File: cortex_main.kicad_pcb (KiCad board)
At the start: 2 copper layers, 177.8 x 86.4 mm, 7 parts, among them P1 CONN_01X05, P2 CONN_02X04, P3 CONN_01X02, U1 socket_leon_x3_dil64, U2 socket_pololu_24v12, U3 socket_pololu_24v12, U4 socket_lm2596_mod

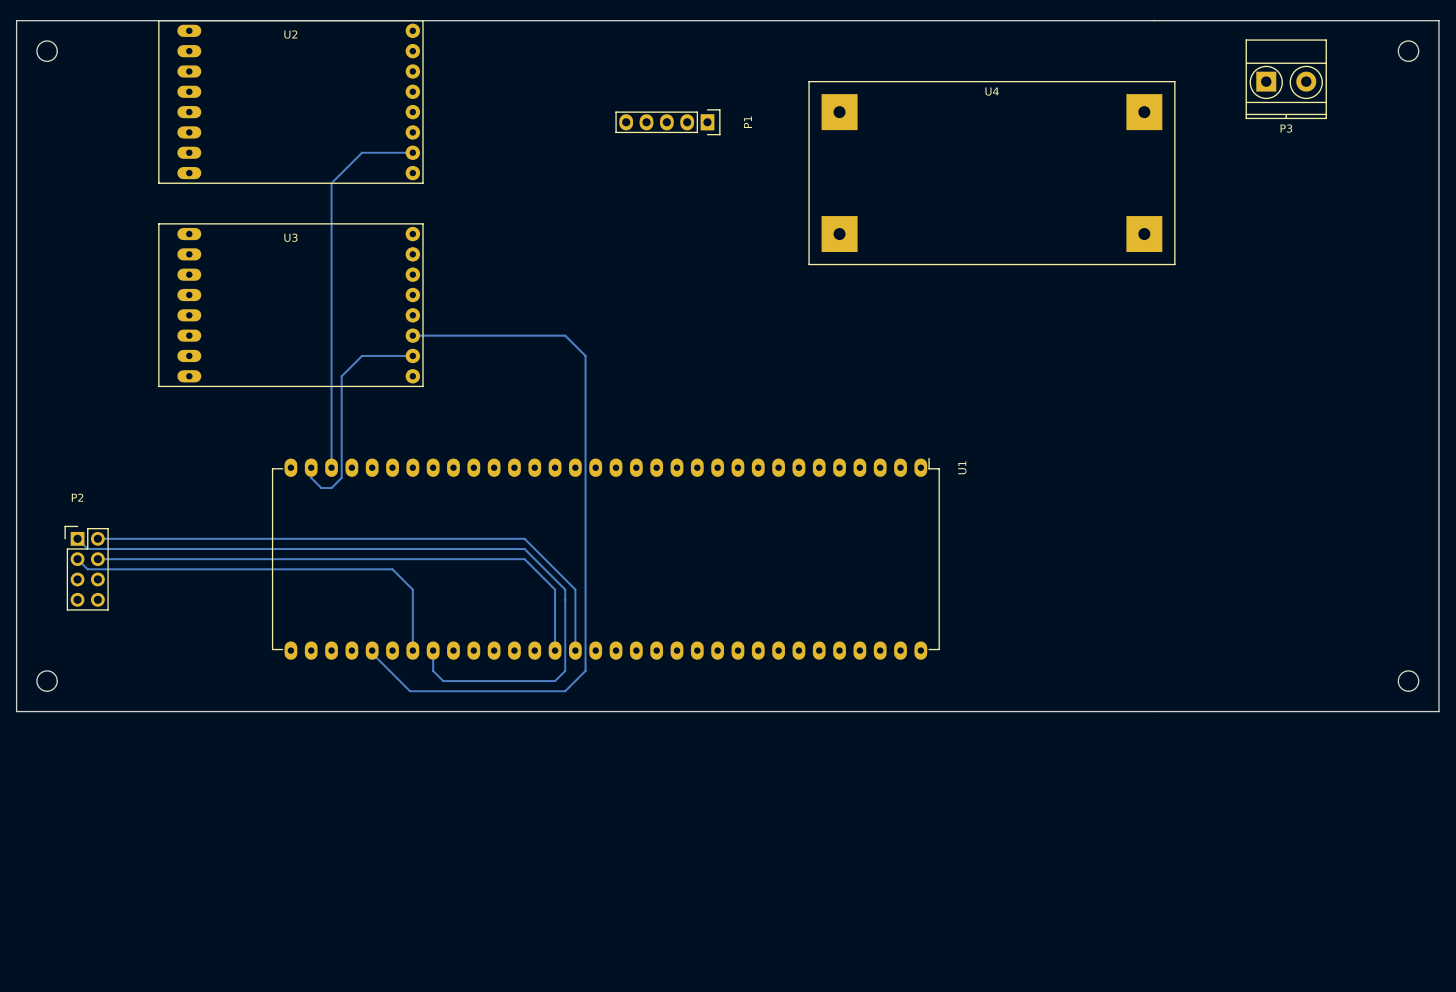
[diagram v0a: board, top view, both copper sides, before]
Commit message: cortex: update to 120x120mm PCB size
To match final mechanical constraints

Signed-off-by: Yannick Gicquel <ygicquel@gmail.com>
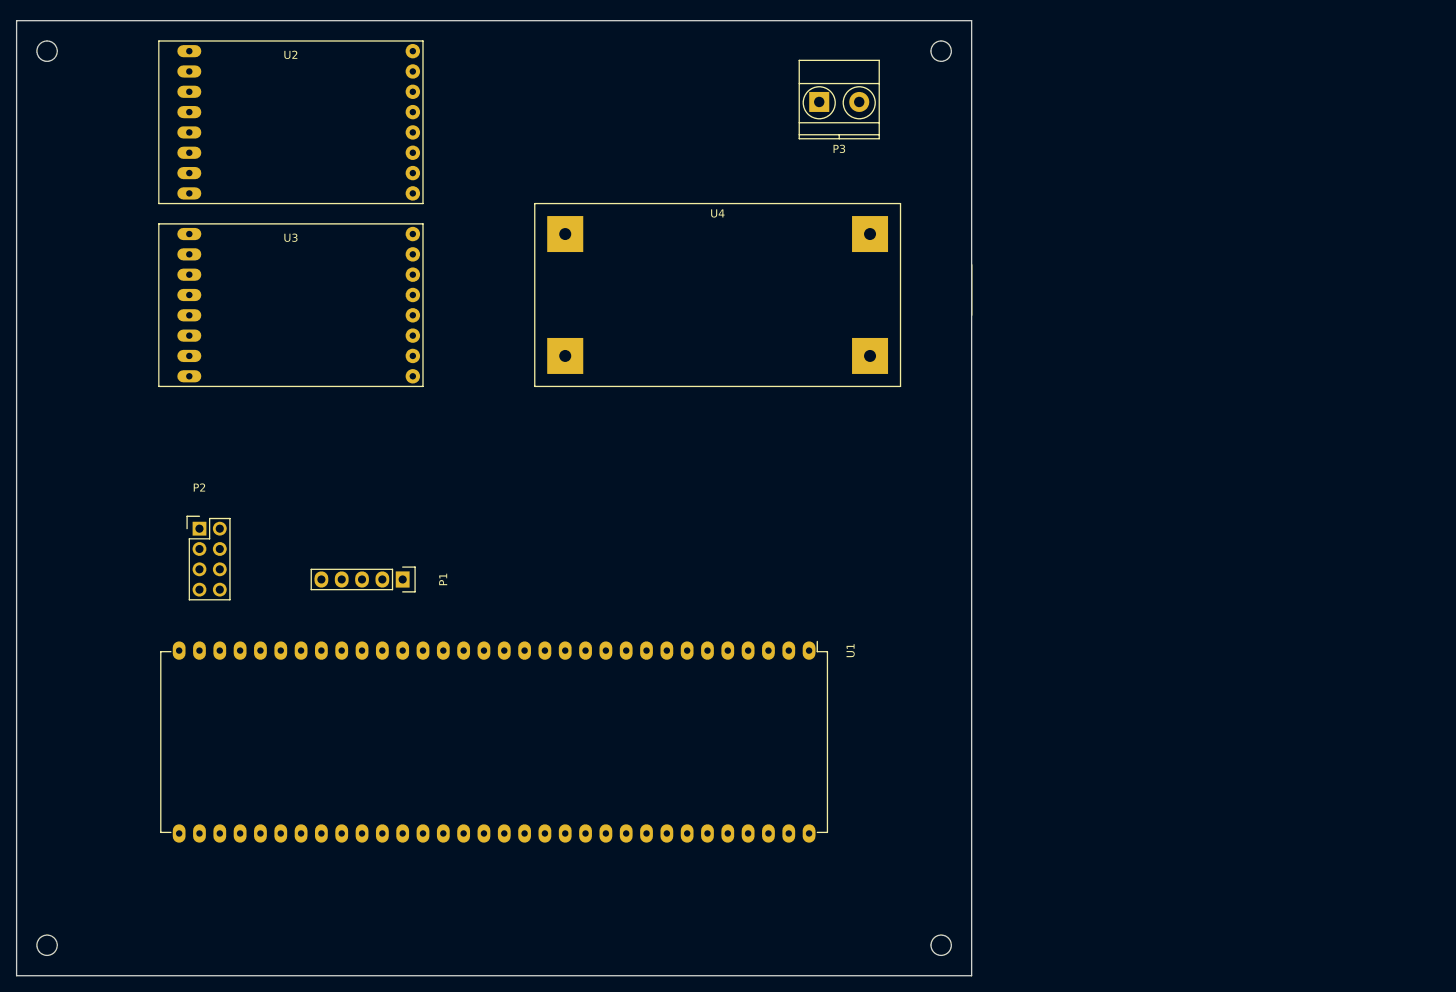
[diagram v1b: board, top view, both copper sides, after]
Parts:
- moved P1 68.7 mm to (83.8, 119.4)
- moved P3 55.9 mm to (135.9, 59.7)
- moved U4 37.5 mm to (123.2, 83.8)
- moved U1 26.8 mm to (134.6, 128.3)
- moved P2 15.3 mm to (58.4, 113.0)
- moved U2 2.54 mm to (69.8, 62.2)
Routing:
- net ENCB_L: track 93.9 -> 0.00 mm
- net /Sheet_MCU/PWM_R: track 92.0 -> 0.35 mm
- net ENCB_R: track 69.9 -> 0.00 mm
- net ENCA_R: track 66.3 -> 0.00 mm
- net ENCA_L: track 51.1 -> 0.00 mm
- net /Sheet_MCU/DIR_L: track 47.3 -> 0.00 mm
- net /Sheet_MCU/DIR_R: track 28.8 -> 0.00 mm
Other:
- board size 177.8 x 86.4 mm -> 119.4 x 119.4 mm

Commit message: cortex: add 3V3 regulator
Signed-off-by: Yannick Gicquel <ygicquel@gmail.com>
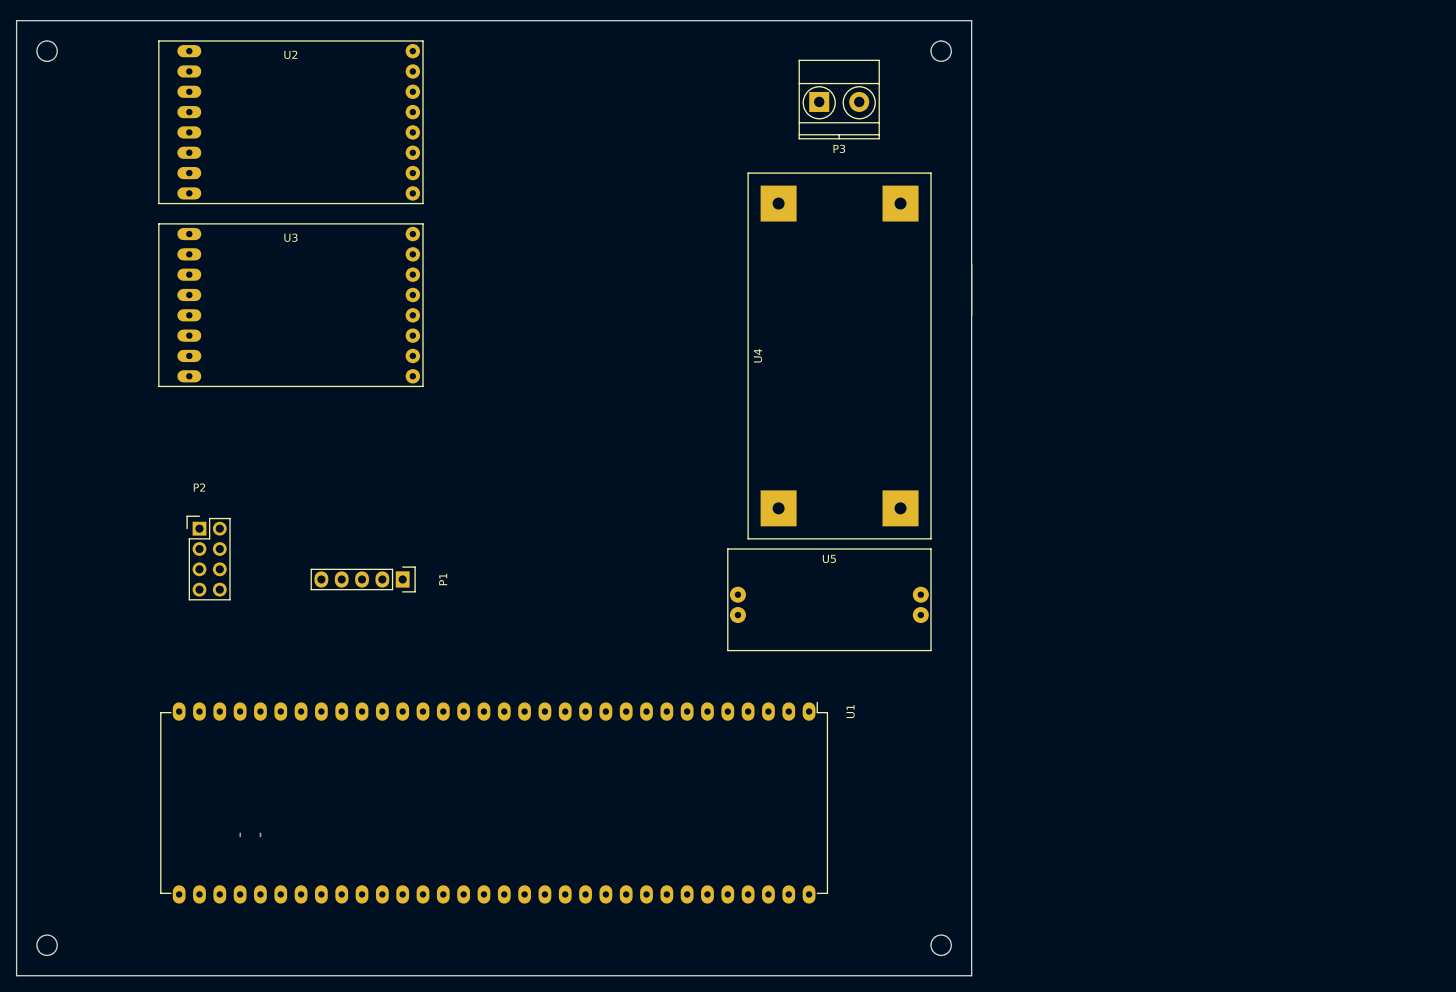
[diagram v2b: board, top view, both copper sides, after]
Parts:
- added U5: socket_ams1117-3V3_mod, bot_parts:ams1117-3V3_mod, F.Cu at (137.2, 121.9)
- moved U4 17.0 mm to (138.4, 91.4), turned to 270 degrees
- moved U1 7.62 mm to (134.6, 135.9)
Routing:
- net (no net): track 0.00 -> 0.70 mm
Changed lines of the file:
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@@
 (kicad_pcb (version 4) (host pcbnew 4.0.5-e0-6337~49~ubuntu16.04.1)
   (general
-    (links 35)
-    (no_connects 35)
-    (area 35.484999 49.254999 213.435001 135.965001)
+    (links 39)
+    (no_connects 39)
+    (area 35.484999 49.454999 155.015001 168.985001)
     (thickness 1.6)
     (drawings 9)
     (tracks 2)
     (zones 0)
-    (modules 7)
+    (modules 8)
     (nets 81)
   )
@@
   )
   (module Housings_DIP:DIP-64_W22.86mm_LongPads (layer F.Cu)
-    (at 134.62 128.27 270)
+    (at 134.62 135.89 270)
     (descr "64-lead dip package, row spacing 22.86 mm (900 mils), longer pads")
     (tags "dil dip 2.54 900")
@@
   )
   (module bot_parts:lm2596s_mod (layer F.Cu)
-    (at 123.19 83.82 180)
-    (fp_text reference U4 (at 0 10.16 180) (layer F.SilkS)
-      (effects (font (size 1 1) (thickness 0.15)))
-    )
-    (fp_text value socket_lm2596_mod (at 0 -10.16 180) (layer F.Fab)
+    (at 138.43 91.44 270)
+    (fp_text reference U4 (at 0 10.16 270) (layer F.SilkS)
+      (effects (font (size 1 1) (thickness 0.15)))
+    )
+    (fp_text value socket_lm2596_mod (at 0 -10.16 270) (layer F.Fab)
       (effects (font (size 1 1) (thickness 0.15)))
     )
@@
     (fp_line (start 22.86 11.43) (end -22.86 11.43) (layer F.SilkS) (width 0.15))
     (fp_line (start -22.86 11.43) (end -22.86 -11.43) (layer F.SilkS) (width 0.15))
-    (pad 1 thru_hole rect (at -19.05 -7.62 180) (size 4.5 4.5) (drill 1.5) (layers *.Cu *.Mask)
-      (net 61 +24V))
-    (pad 2 thru_hole rect (at -19.05 7.62 180) (size 4.5 4.5) (drill 1.5) (layers *.Cu *.Mask)
-      (net 62 GND))
-    (pad 3 thru_hole rect (at 19.05 -7.62 180) (size 4.5 4.5) (drill 1.5) (layers *.Cu *.Mask)
+    (pad 1 thru_hole rect (at -19.05 -7.62 270) (size 4.5 4.5) (drill 1.5) (layers *.Cu *.Mask)
+      (net 61 +24V))
+    (pad 2 thru_hole rect (at -19.05 7.62 270) (size 4.5 4.5) (drill 1.5) (layers *.Cu *.Mask)
+      (net 62 GND))
+    (pad 3 thru_hole rect (at 19.05 -7.62 270) (size 4.5 4.5) (drill 1.5) (layers *.Cu *.Mask)
       (net 80 +5V))
-    (pad 4 thru_hole rect (at 19.05 7.62 180) (size 4.5 4.5) (drill 1.5) (layers *.Cu *.Mask)
+    (pad 4 thru_hole rect (at 19.05 7.62 270) (size 4.5 4.5) (drill 1.5) (layers *.Cu *.Mask)
+      (net 62 GND))
+  )
+  (module bot_parts:ams1117-3V3_mod (layer F.Cu)
+    (at 137.16 121.92 180)
+    (fp_text reference U5 (at 0 5.08 180) (layer F.SilkS)
+      (effects (font (size 1 1) (thickness 0.15)))
+    )
+    (fp_text value socket_ams1117-3V3_mod (at 0 -5.08 180) (layer F.Fab)
+      (effects (font (size 1 1) (thickness 0.15)))
+    )
+    (fp_line (start -12.7 -6.35) (end 12.7 -6.35) (layer F.SilkS) (width 0.15))
+    (fp_line (start 12.7 -6.35) (end 12.7 6.35) (layer F.SilkS) (width 0.15))
+    (fp_line (start 12.7 6.35) (end -12.7 6.35) (layer F.SilkS) (width 0.15))
+    (fp_line (start -12.7 6.35) (end -12.7 -6.35) (layer F.SilkS) (width 0.15))
+    (pad 1 thru_hole circle (at -11.43 -1.905 180) (size 2 2) (drill 0.8) (layers *.Cu *.Mask)
+      (net 80 +5V))
+    (pad 2 thru_hole circle (at -11.43 0.635 180) (size 2 2) (drill 0.8) (layers *.Cu *.Mask)
+      (net 62 GND))
+    (pad 3 thru_hole circle (at 11.43 -1.905 180) (size 2 2) (drill 0.8) (layers *.Cu *.Mask)
+      (net 63 +3V3))
+    (pad 4 thru_hole circle (at 11.43 0.635 180) (size 2 2) (drill 0.8) (layers *.Cu *.Mask)
       (net 62 GND))
   )
@@
   (gr_circle (center 151.13 165.1) (end 152.4 165.1) (layer Edge.Cuts) (width 0.15))
   (gr_circle (center 39.37 165.1) (end 40.64 165.1) (layer Edge.Cuts) (width 0.15))
-  (segment (start 63.5 151.13) (end 63.5 151.48) (width 0.25) (layer B.Cu) (net 74))
-  (segment (start 66.04 151.13) (end 66.04 151.48) (width 0.25) (layer B.Cu) (net 75))
+  (segment (start 63.5 151.13) (end 63.5 151.48) (width 0.25) (layer B.Cu) (net 0))
+  (segment (start 66.04 151.13) (end 66.04 151.48) (width 0.25) (layer B.Cu) (net 0))
 )

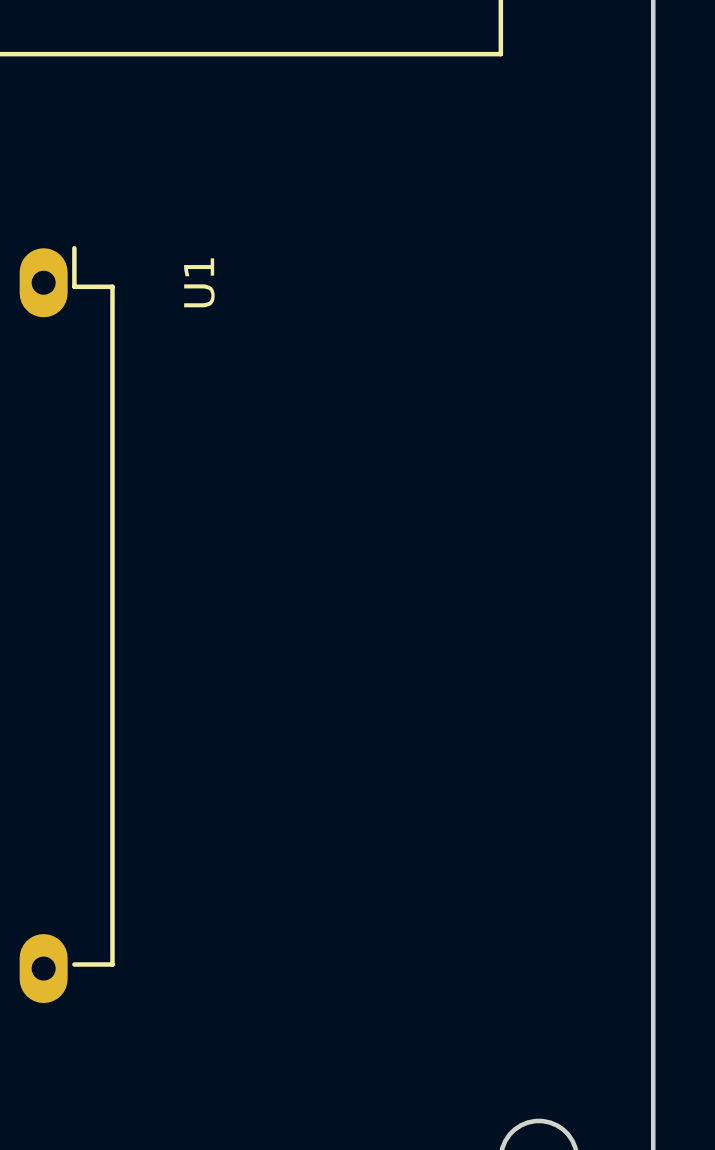
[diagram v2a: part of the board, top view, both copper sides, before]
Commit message: cortex: add I2C bus & connectors to SD21 extension board
Signed-off-by: Yannick Gicquel <ygicquel@gmail.com>
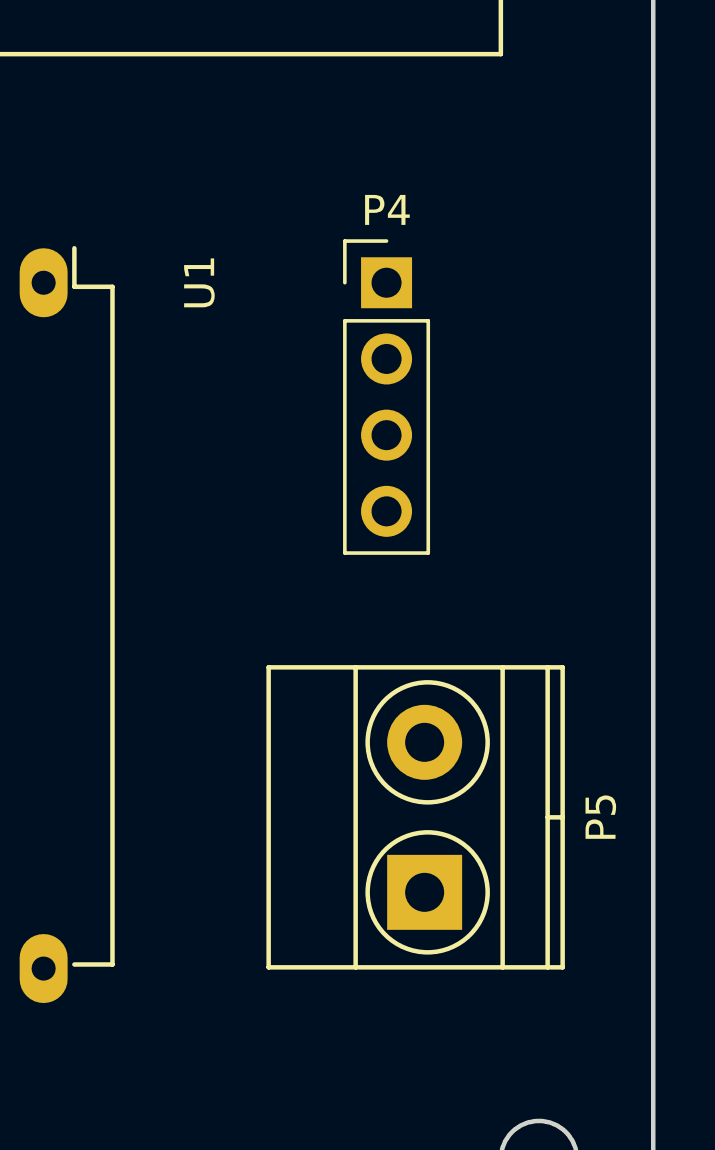
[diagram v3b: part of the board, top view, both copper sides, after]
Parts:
- added P4: CONN_01X04, Pin_Headers:Pin_Header_Straight_1x04_Pitch2.54mm, F.Cu at (146.1, 135.9)
- added P5: CONN_01X02, Terminal_Blocks:TerminalBlock_Pheonix_MKDS1.5-2pol, F.Cu at (147.3, 156.2)
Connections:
- U1 pad 16: Net-(U1-Pad16) -> /Sheet_Connectors/SDA
- U1 pad 17: Net-(U1-Pad17) -> /Sheet_Connectors/SCL
- U1 pad 39: ENCA_L -> Net-(U1-Pad39)
- U1 pad 40: ENCB_L -> ENCA_L
- U1 pad 41: Net-(U1-Pad41) -> ENCB_L

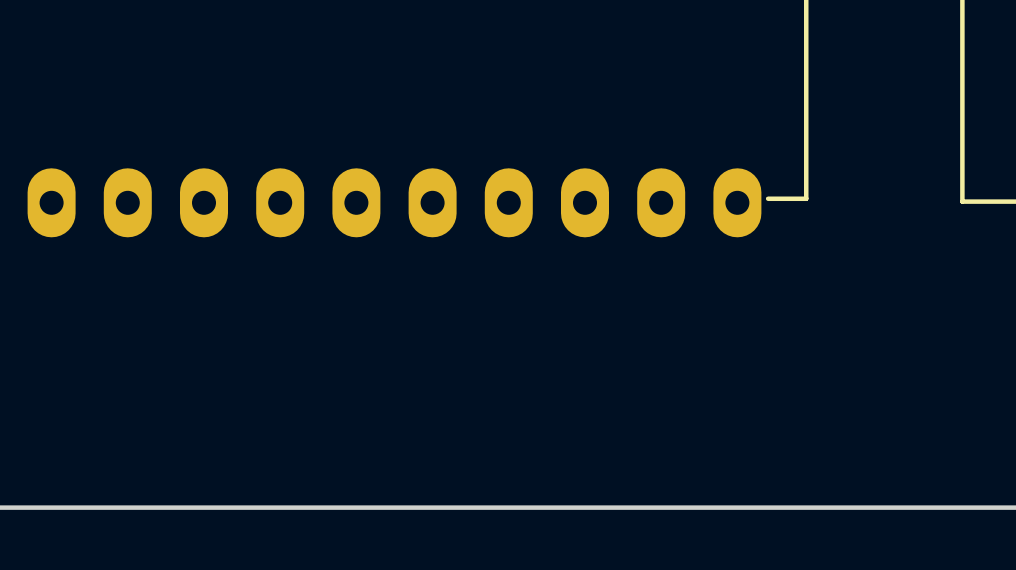
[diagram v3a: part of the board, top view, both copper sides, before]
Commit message: cortex: add MCP100-D to reset MCU
Signed-off-by: Yannick Gicquel <ygicquel@gmail.com>
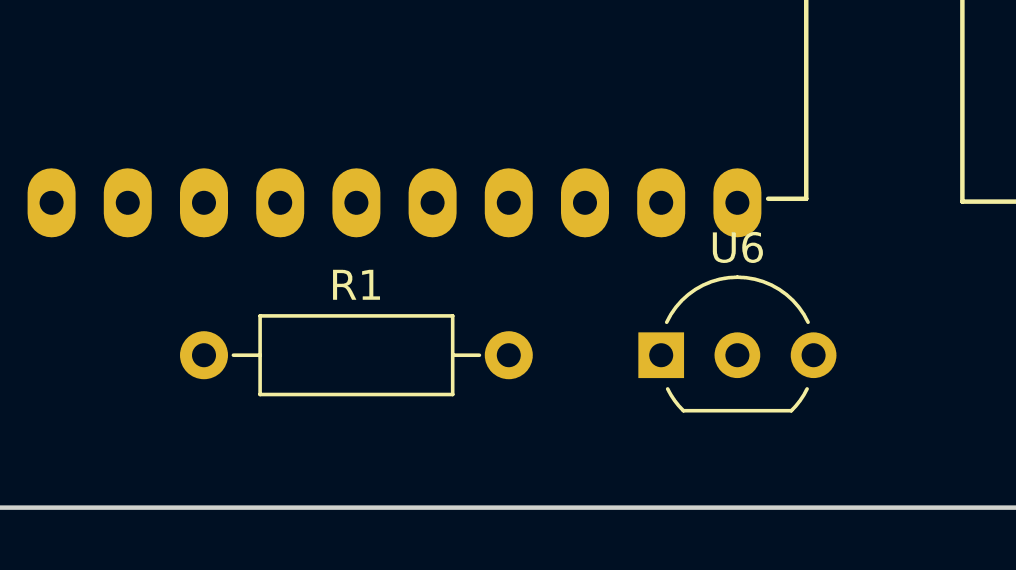
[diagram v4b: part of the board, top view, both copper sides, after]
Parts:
- added R1: 1K, Resistors_ThroughHole:R_Axial_DIN0207_L6.3mm_D2.5mm_P10.16mm_Horizontal, F.Cu at (116.8, 163.8)
- added U6: MCP100-D, bot_parts:TO-92_Inline_Wide, F.Cu at (132.1, 163.8)
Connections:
- U1 pad 14: Net-(U1-Pad14) -> GND
- U1 pad 15: Net-(U1-Pad15) -> +3V3
- U1 pad 24: Net-(U1-Pad24) -> GND
- U1 pad 25: Net-(U1-Pad25) -> +3V3
- U1 pad 34: Net-(U1-Pad34) -> GND
- U1 pad 35: Net-(U1-Pad35) -> +3V3
- U1 pad 44: Net-(U1-Pad44) -> GND
- U1 pad 45: Net-(U1-Pad45) -> +3V3
- U1 pad 52: Net-(U1-Pad52) -> GND
- U1 pad 53: Net-(U1-Pad53) -> +3V3
- U1 pad 60: Net-(U1-Pad60) -> GND
- U1 pad 61: Net-(U1-Pad61) -> +3V3
